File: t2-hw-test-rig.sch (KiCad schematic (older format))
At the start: 21 parts

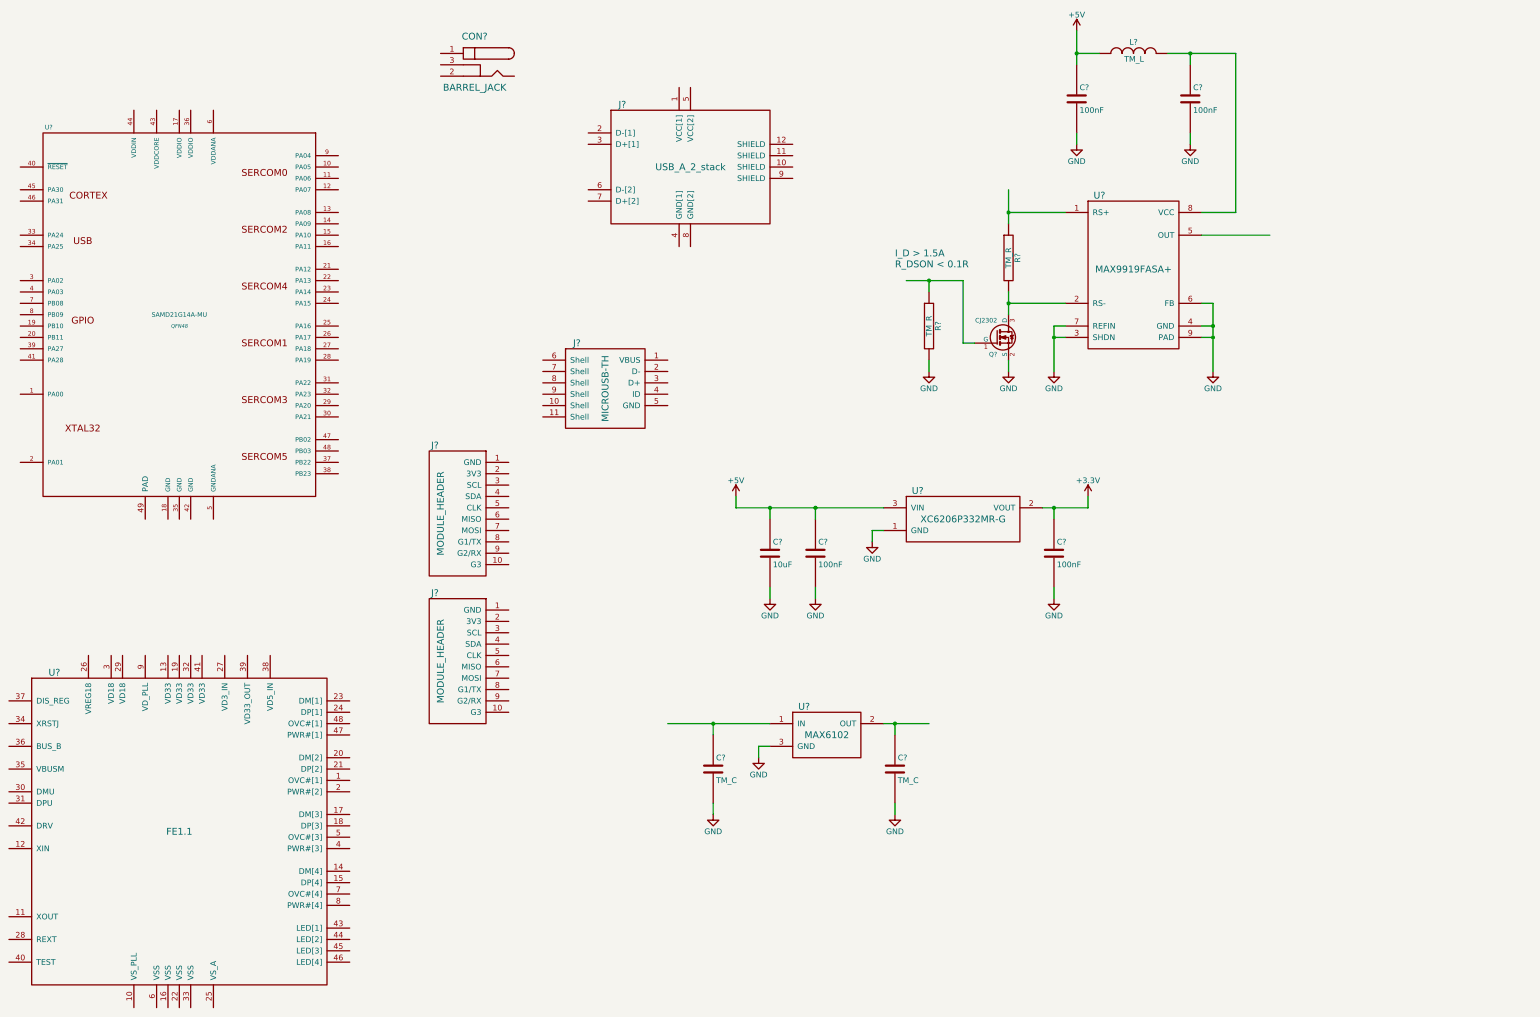
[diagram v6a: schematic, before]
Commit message: broke out usb and sam to sheets
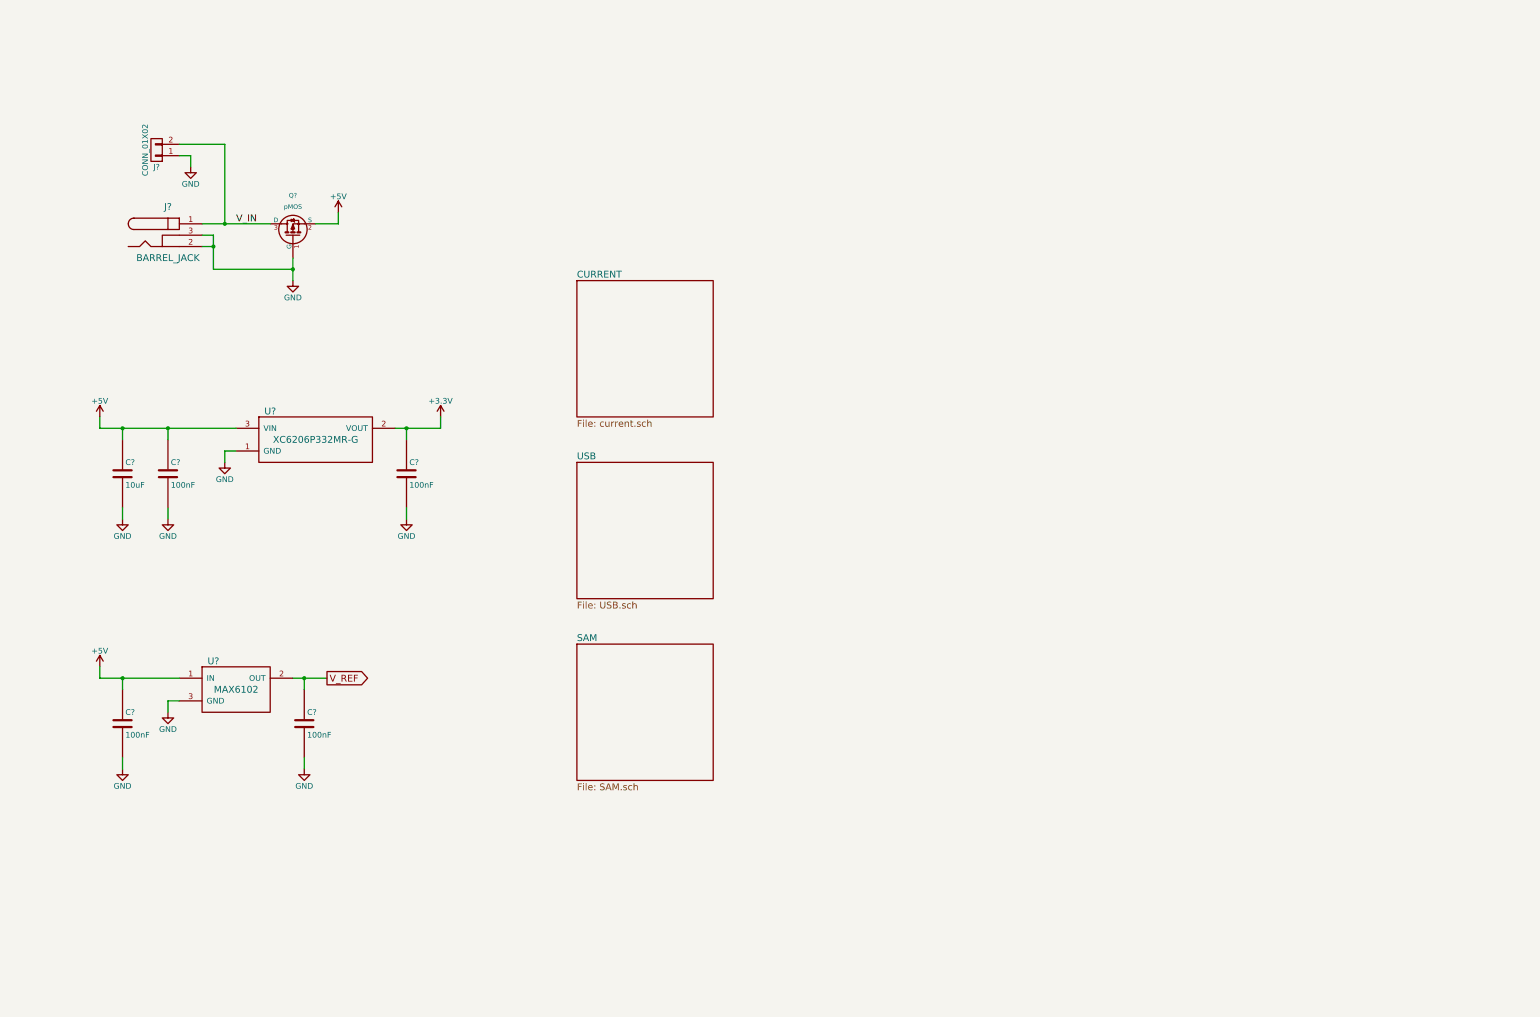
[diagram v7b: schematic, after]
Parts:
- removed C? (x2): 100nF, symbol TM_C
- removed CON?: BARREL_JACK, symbol BARREL_JACK
- removed J?: USB_A_2_stack, symbol USB_A_2_stack
- removed J?: MICROUSB-TH, symbol MICROUSB-TH
- removed J? (x2): MODULE_HEADER, symbol MODULE_HEADER
- removed L?: TM_L, symbol TM_L
- removed Q?: CJ2302, symbol nMOS
- removed R? (x2): TM_R, symbol TM_R
- removed U?: SAMD21G14A-MU, QFN48, symbol SAMD21G14A-MU
- removed U?: FE1.1, symbol FE1.1
- removed U?: MAX9919FASA+, symbol MAX9919
- added J?: BARREL_JACK, symbol BARREL_JACK
- added J?: CONN_01X02, symbol CONN_01X02
- added Q?: pMOS, FOOTPRINT, symbol pMOS
- C? (x2): value TM_C -> 100nF
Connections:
- net labels added: V_IN, V_REF
- wire segments 59 -> 41
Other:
- note removed: "I_D > 1.5A\nR_DSON < 0.1R"
- moved on the sheet: C?, U?

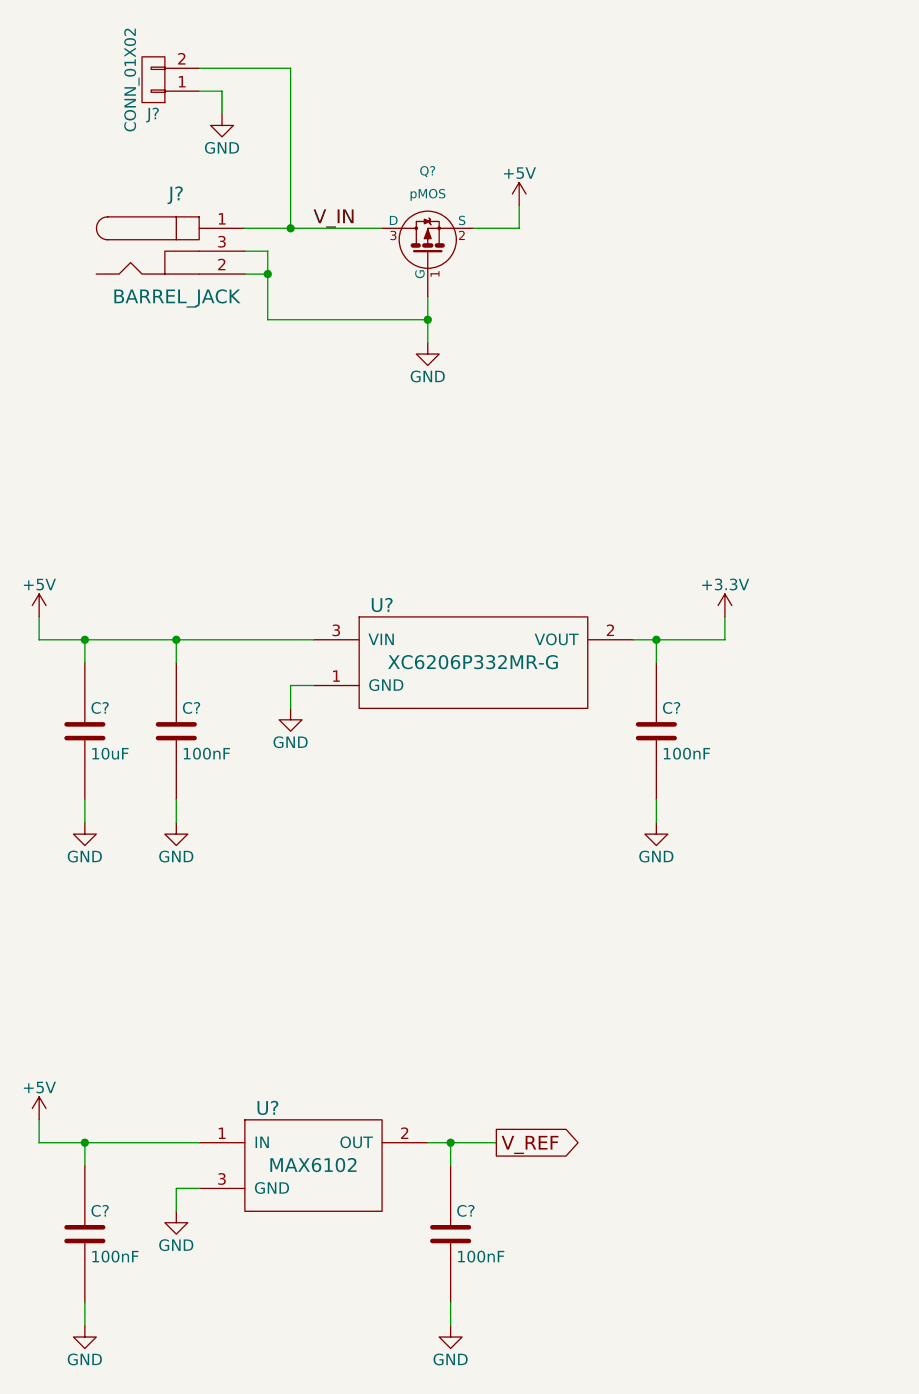
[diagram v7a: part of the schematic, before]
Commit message: ...and now the schematics are in git
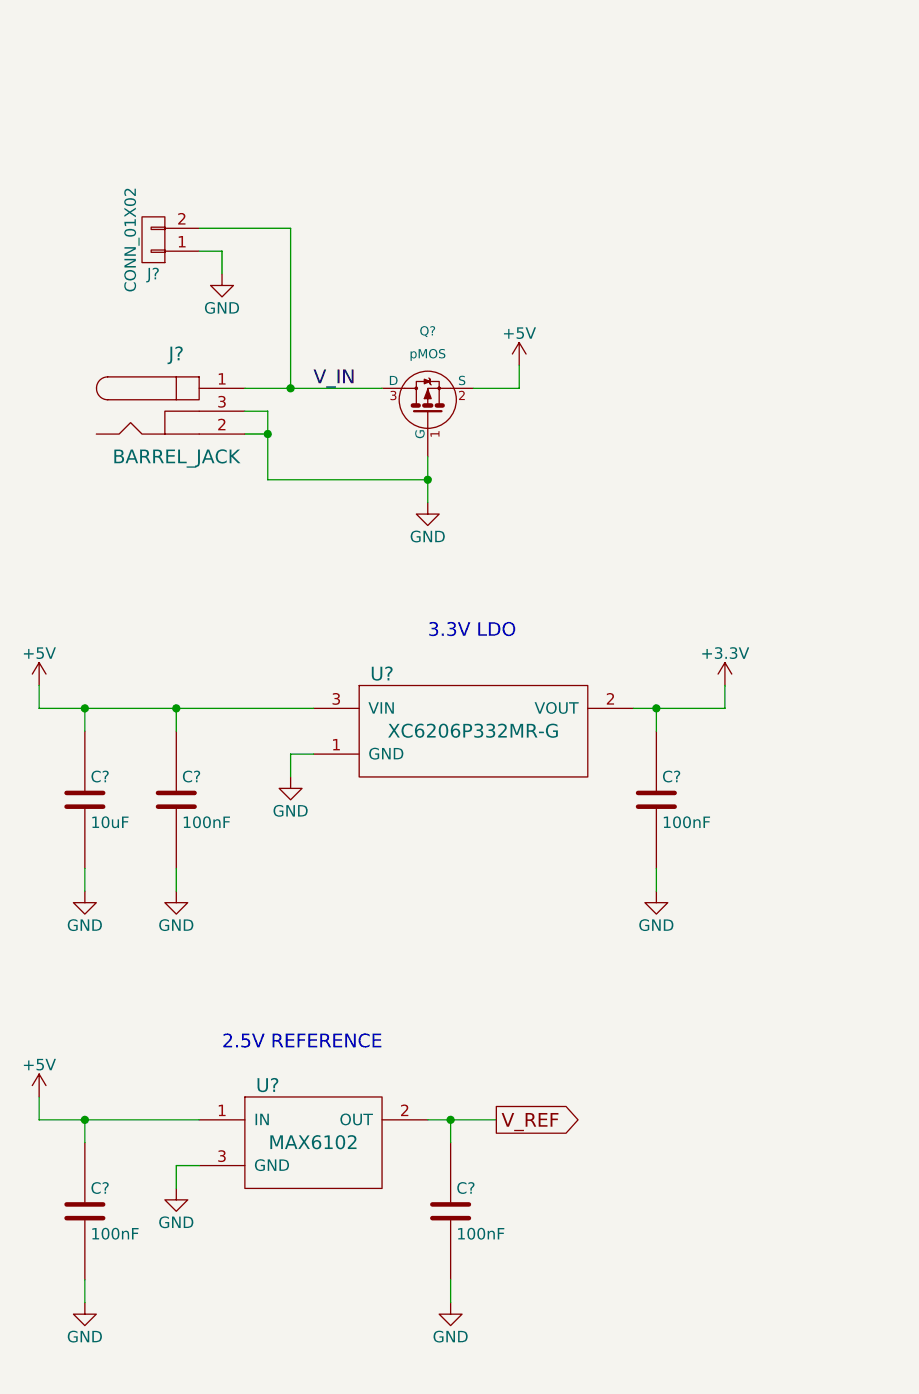
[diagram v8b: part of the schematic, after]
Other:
- note added: "2.5V REFERENCE"
- note added: "3.3V LDO"
- moved on the sheet: C?, J?, Q?, U?
